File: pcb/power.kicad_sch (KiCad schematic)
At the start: 16 parts, among them J3 USB_C_Receptacle_USB2.0, J4 Barrel_Jack_Switch, U10 LTC4054ES5-4.2, U7 TLV1117-50, U8 XC6206PxxxMR, U9 SRV05-4

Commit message: v2
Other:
- moved on the sheet: J4

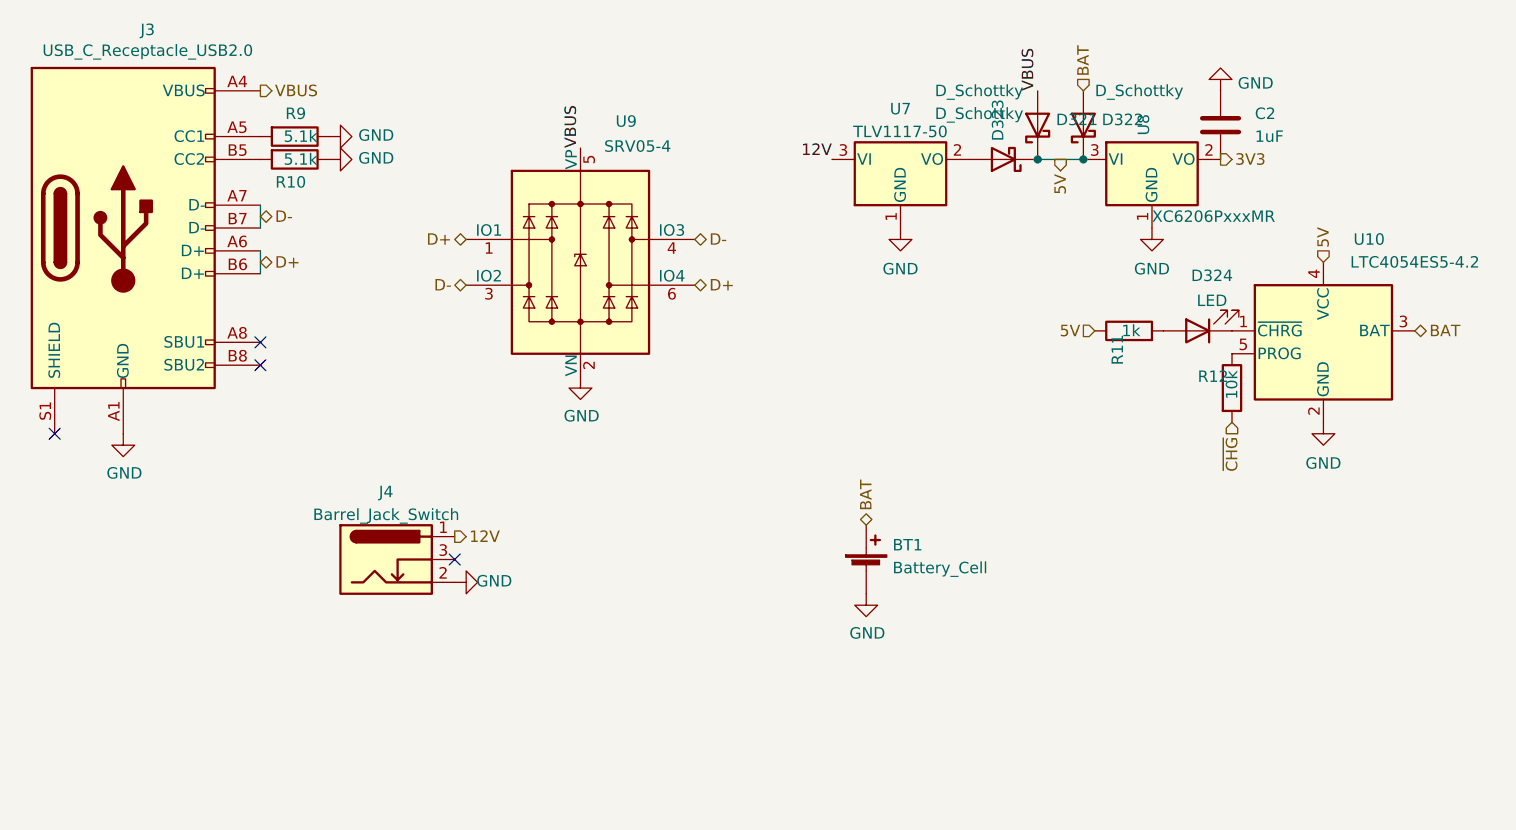
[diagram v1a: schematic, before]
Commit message: stamp ground vias; ERC
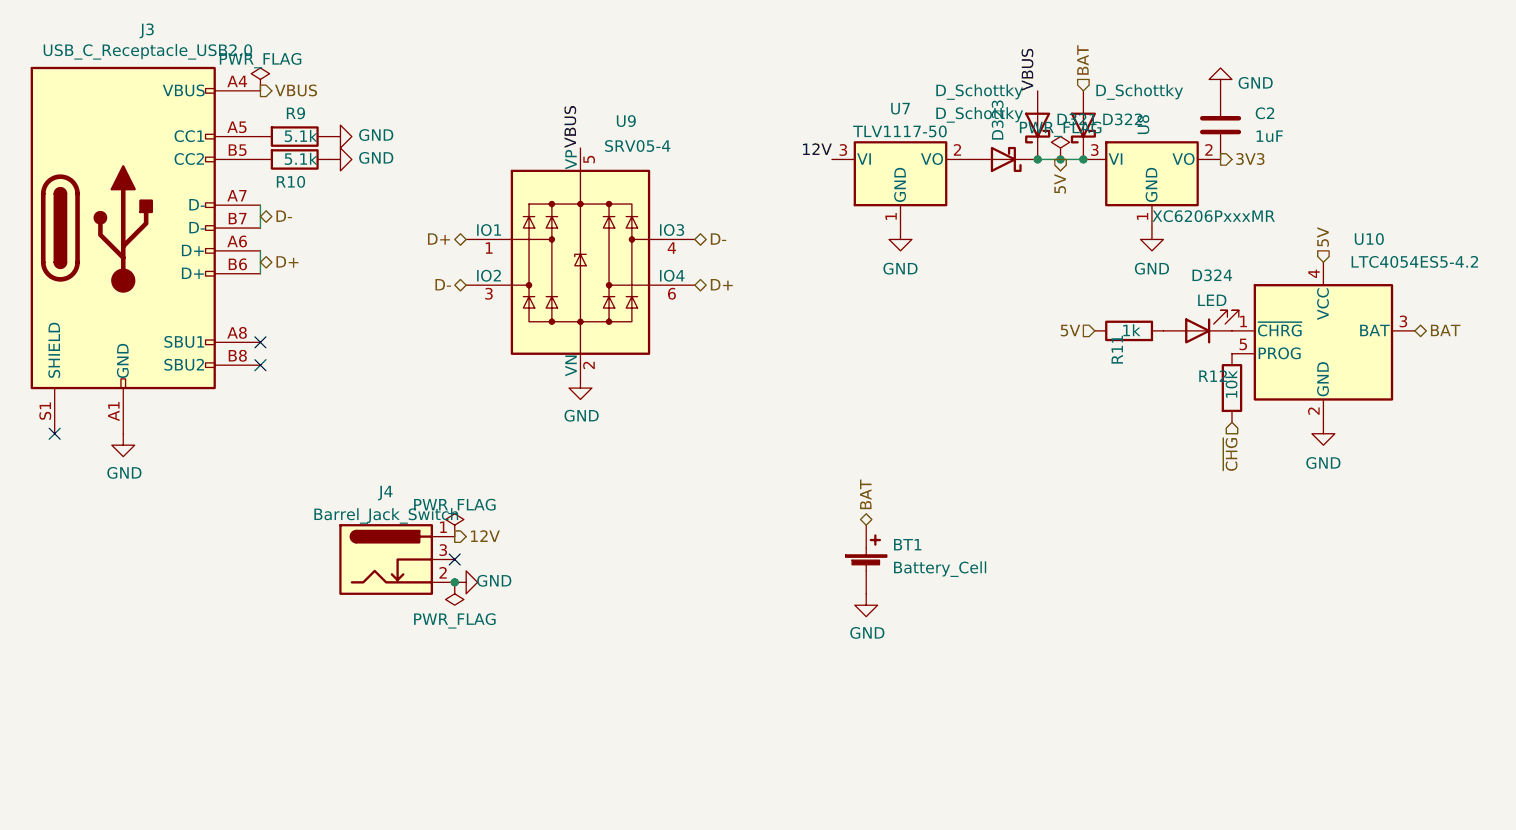
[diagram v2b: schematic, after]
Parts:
- U8: footprint Package_TO_SOT_SMD:SOT-23 -> Package_TO_SOT_SMD:SOT-23-3
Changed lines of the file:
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@@
 (kicad_sch (version 20230121) (generator eeschema)
   (paper "A4")
+  (junction (at 72.39 80.01) (diameter 0) (color 0 0 0 0)
+  )
   (junction (at 142.24 33.02) (diameter 0) (color 0 0 0 0)
   )
   (junction (at 137.16 33.02) (diameter 0) (color 0 0 0 0)
+  )
+  (junction (at 139.7 33.02) (diameter 0) (color 0 0 0 0)
   )
   (no_connect (at 27.94 63.5))
@@
     (stroke (width 0) (type solid))
   )
-  (wire (pts (xy 137.16 33.02) (xy 142.24 33.02))
+  (wire (pts (xy 137.16 33.02) (xy 139.7 33.02))
     (stroke (width 0) (type default))
   )
@@
     (stroke (width 0) (type solid))
   )
+  (wire (pts (xy 139.7 33.02) (xy 142.24 33.02))
+    (stroke (width 0) (type default))
+  )
   (label "12V" (at 114.3 33.02 180) (fields_autoplaced)
     (effects (font (size 1.27 1.27)) (justify right bottom))
@@
     (effects (font (size 1.27 1.27)) (justify right))
   )
+  (symbol (lib_id "power:PWR_FLAG") (at 139.7 33.02 0) (unit 1)
+    (in_bom yes) (on_board yes) (dnp no) (fields_autoplaced)
+    (property "Reference" "#FLG04" (at 139.7 31.115 0)
+      (effects (font (size 1.27 1.27)) hide)
+    )
+    (property "Value" "PWR_FLAG" (at 139.7 29.5181 0)
+      (effects (font (size 1.27 1.27)))
+    )
+    (property "Footprint" "" (at 139.7 33.02 0)
+      (effects (font (size 1.27 1.27)) hide)
+    )
+    (property "Datasheet" "~" (at 139.7 33.02 0)
+      (effects (font (size 1.27 1.27)) hide)
+    )
+    (pin "1")
+    (instances
+      (project "zeub"
+        (path "/e63e39d7-6ac0-4ffd-8aa3-1841a4541b55/79d57789-5a81-4689-bd1f-5ca26896f57e"
+          (reference "#FLG04") (unit 1)
+        )
+      )
+    )
+  )
   (symbol (lib_id "Regulator_Linear:XC6206PxxxMR") (at 149.86 33.02 0) (unit 1)
     (in_bom yes) (on_board yes) (dnp no)
@@
       (effects (font (size 1.27 1.27)) (justify left))
     )
-    (property "Footprint" "Package_TO_SOT_SMD:SOT-23" (at 149.86 27.305 0)
+    (property "Footprint" "Package_TO_SOT_SMD:SOT-23-3" (at 149.86 27.305 0)
       (effects (font (size 1.27 1.27) italic) hide)
     )
@@
     )
   )
+  (symbol (lib_id "power:PWR_FLAG") (at 50.8 25.4 0) (unit 1)
+    (in_bom yes) (on_board yes) (dnp no) (fields_autoplaced)
+    (property "Reference" "#FLG02" (at 50.8 23.495 0)
+      (effects (font (size 1.27 1.27)) hide)
+    )
+    (property "Value" "PWR_FLAG" (at 50.8 21.8981 0)
+      (effects (font (size 1.27 1.27)))
+    )
+    (property "Footprint" "" (at 50.8 25.4 0)
+      (effects (font (size 1.27 1.27)) hide)
+    )
+    (property "Datasheet" "~" (at 50.8 25.4 0)
+      (effects (font (size 1.27 1.27)) hide)
+    )
+    (pin "1")
+    (instances
+      (project "zeub"
+        (path "/e63e39d7-6ac0-4ffd-8aa3-1841a4541b55/79d57789-5a81-4689-bd1f-5ca26896f57e"
+          (reference "#FLG02") (unit 1)
+        )
+      )
+    )
+  )
   (symbol (lib_id "power:GND") (at 35.56 63.5 0) (unit 1)
     (in_bom yes) (on_board yes) (dnp no)
@@
     )
   )
+  (symbol (lib_id "power:PWR_FLAG") (at 72.39 80.01 180) (unit 1)
+    (in_bom yes) (on_board yes) (dnp no) (fields_autoplaced)
+    (property "Reference" "#FLG03" (at 72.39 81.915 0)
+      (effects (font (size 1.27 1.27)) hide)
+    )
+    (property "Value" "PWR_FLAG" (at 72.39 84.1455 0)
+      (effects (font (size 1.27 1.27)))
+    )
+    (property "Footprint" "" (at 72.39 80.01 0)
+      (effects (font (size 1.27 1.27)) hide)
+    )
+    (property "Datasheet" "~" (at 72.39 80.01 0)
+      (effects (font (size 1.27 1.27)) hide)
+    )
+    (pin "1")
+    (instances
+      (project "zeub"
+        (path "/e63e39d7-6ac0-4ffd-8aa3-1841a4541b55/79d57789-5a81-4689-bd1f-5ca26896f57e"
+          (reference "#FLG03") (unit 1)
+        )
+      )
+    )
+  )
   (symbol (lib_id "Regulator_Linear:TLV1117-50") (at 121.92 33.02 0) (unit 1)
     (in_bom yes) (on_board yes) (dnp no) (fields_autoplaced)
@@
         )
       )
+    )
+  )
+  (symbol (lib_id "power:PWR_FLAG") (at 72.39 74.93 0) (unit 1)
+    (in_bom yes) (on_board yes) (dnp no) (fields_autoplaced)
+    (property "Reference" "#FLG01" (at 72.39 73.025 0)
+      (effects (font (size 1.27 1.27)) hide)
+    )
+    (property "Value" "PWR_FLAG" (at 72.39 71.4281 0)
+      (effects (font (size 1.27 1.27)))
+    )
+    (property "Footprint" "" (at 72.39 74.93 0)
+      (effects (font (size 1.27 1.27)) hide)
+    )
+    (property "Datasheet" "~" (at 72.39 74.93 0)
+      (effects (font (size 1.27 1.27)) hide)
+    )
+    (pin "1")
+    (instances
+      (project "zeub"
+        (path "/e63e39d7-6ac0-4ffd-8aa3-1841a4541b55/79d57789-5a81-4689-bd1f-5ca26896f57e"
+          (reference "#FLG01") (unit 1)
+        )
+      )
